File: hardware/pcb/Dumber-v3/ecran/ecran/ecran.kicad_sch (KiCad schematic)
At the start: 14 parts, among them J1 TE 1-84981-0

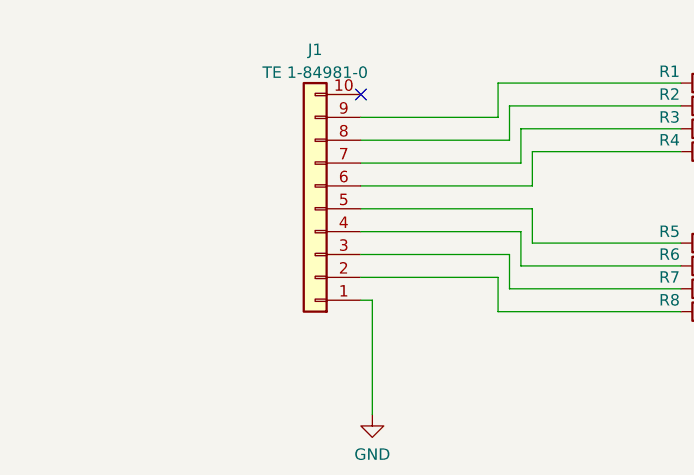
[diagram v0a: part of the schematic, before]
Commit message: asservissement moteur de base OK
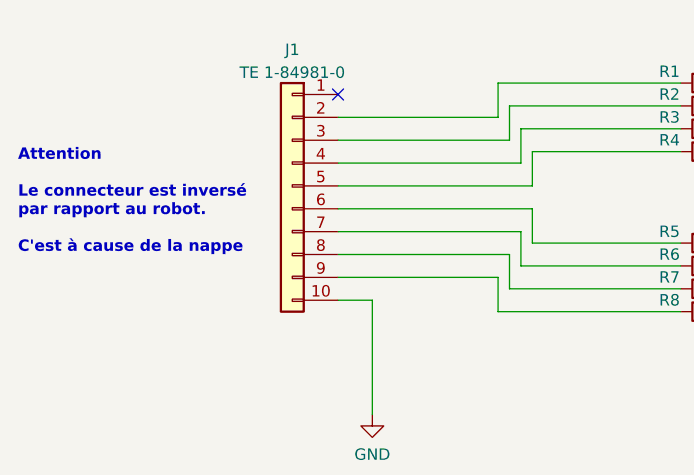
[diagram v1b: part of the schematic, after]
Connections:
- net GND: now also J1.10 (Pin_10); no longer J1.1 (Pin_1)
- net at R8.1: now also J1.9 (Pin_9); no longer J1.2 (Pin_2)
- net at R1.1: now also J1.2 (Pin_2); no longer J1.9 (Pin_9)
- net at R2.1: now also J1.3 (Pin_3); no longer J1.8 (Pin_8)
- net at R6.1: now also J1.7 (Pin_7); no longer J1.4 (Pin_4)
- net at R4.1: now also J1.5 (Pin_5); no longer J1.6 (Pin_6)
- net at R7.1: now also J1.8 (Pin_8); no longer J1.3 (Pin_3)
- net at R5.1: now also J1.6 (Pin_6); no longer J1.5 (Pin_5)
- net at R3.1: now also J1.4 (Pin_4); no longer J1.7 (Pin_7)
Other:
- note added: "Attention Le connecteur est inversé par rapport au robot. C'est à cause de la nappe"
- moved on the sheet: J1
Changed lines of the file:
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@@
     (company "INSA - GEI")
   )
+  (no_connect (at 58.42 63.5))
   (no_connect (at 175.26 86.36))
-  (no_connect (at 60.96 63.5))
   (wire (pts (xy 148.59 83.82) (xy 119.38 83.82))
     (stroke (width 0) (type default) (color 0 0 0 0))
@@
     (stroke (width 0) (type default) (color 0 0 0 0))
   )
+  (wire (pts (xy 58.42 81.28) (xy 77.47 81.28))
+    (stroke (width 0) (type default) (color 0 0 0 0))
+  )
   (wire (pts (xy 62.23 86.36) (xy 62.23 99.06))
     (stroke (width 0) (type default) (color 0 0 0 0))
   )
-  (wire (pts (xy 60.96 76.2) (xy 80.01 76.2))
-    (stroke (width 0) (type default) (color 0 0 0 0))
-  )
-  (wire (pts (xy 60.96 71.12) (xy 78.74 71.12))
-    (stroke (width 0) (type default) (color 0 0 0 0))
-  )
   (wire (pts (xy 104.14 82.55) (xy 110.49 82.55))
     (stroke (width 0) (type default) (color 0 0 0 0))
   )
-  (wire (pts (xy 60.96 66.04) (xy 76.2 66.04))
-    (stroke (width 0) (type default) (color 0 0 0 0))
-  )
   (wire (pts (xy 78.74 67.31) (xy 96.52 67.31))
     (stroke (width 0) (type default) (color 0 0 0 0))
@@
     (stroke (width 0) (type default) (color 0 0 0 0))
   )
-  (wire (pts (xy 60.96 68.58) (xy 77.47 68.58))
-    (stroke (width 0) (type default) (color 0 0 0 0))
-  )
   (wire (pts (xy 148.59 66.04) (xy 175.26 66.04))
     (stroke (width 0) (type default) (color 0 0 0 0))
@@
     (stroke (width 0) (type default) (color 0 0 0 0))
   )
-  (wire (pts (xy 60.96 81.28) (xy 77.47 81.28))
-    (stroke (width 0) (type default) (color 0 0 0 0))
-  )
   (wire (pts (xy 76.2 87.63) (xy 96.52 87.63))
     (stroke (width 0) (type default) (color 0 0 0 0))
   )
-  (wire (pts (xy 60.96 73.66) (xy 80.01 73.66))
-    (stroke (width 0) (type default) (color 0 0 0 0))
-  )
   (wire (pts (xy 153.67 76.2) (xy 175.26 76.2))
     (stroke (width 0) (type default) (color 0 0 0 0))
@@
     (stroke (width 0) (type default) (color 0 0 0 0))
   )
+  (wire (pts (xy 58.42 66.04) (xy 76.2 66.04))
+    (stroke (width 0) (type default) (color 0 0 0 0))
+  )
+  (wire (pts (xy 58.42 71.12) (xy 78.74 71.12))
+    (stroke (width 0) (type default) (color 0 0 0 0))
+  )
+  (wire (pts (xy 58.42 76.2) (xy 80.01 76.2))
+    (stroke (width 0) (type default) (color 0 0 0 0))
+  )
   (wire (pts (xy 149.86 81.28) (xy 114.3 81.28))
     (stroke (width 0) (type default) (color 0 0 0 0))
@@
     (stroke (width 0) (type default) (color 0 0 0 0))
   )
-  (wire (pts (xy 60.96 78.74) (xy 78.74 78.74))
-    (stroke (width 0) (type default) (color 0 0 0 0))
-  )
   (wire (pts (xy 151.13 71.12) (xy 175.26 71.12))
     (stroke (width 0) (type default) (color 0 0 0 0))
@@
     (stroke (width 0) (type default) (color 0 0 0 0))
   )
+  (wire (pts (xy 58.42 78.74) (xy 78.74 78.74))
+    (stroke (width 0) (type default) (color 0 0 0 0))
+  )
   (wire (pts (xy 119.38 83.82) (xy 119.38 87.63))
     (stroke (width 0) (type default) (color 0 0 0 0))
@@
     (stroke (width 0) (type default) (color 0 0 0 0))
   )
+  (wire (pts (xy 58.42 73.66) (xy 80.01 73.66))
+    (stroke (width 0) (type default) (color 0 0 0 0))
+  )
   (wire (pts (xy 104.14 62.23) (xy 140.97 62.23))
     (stroke (width 0) (type default) (color 0 0 0 0))
@@
     (stroke (width 0) (type default) (color 0 0 0 0))
   )
-  (wire (pts (xy 60.96 83.82) (xy 76.2 83.82))
-    (stroke (width 0) (type default) (color 0 0 0 0))
-  )
   (wire (pts (xy 149.86 68.58) (xy 175.26 68.58))
     (stroke (width 0) (type default) (color 0 0 0 0))
@@
     (stroke (width 0) (type default) (color 0 0 0 0))
   )
+  (wire (pts (xy 58.42 83.82) (xy 76.2 83.82))
+    (stroke (width 0) (type default) (color 0 0 0 0))
+  )
   (wire (pts (xy 104.14 64.77) (xy 142.24 64.77))
     (stroke (width 0) (type default) (color 0 0 0 0))
@@
     (stroke (width 0) (type default) (color 0 0 0 0))
   )
-  (wire (pts (xy 60.96 86.36) (xy 62.23 86.36))
-    (stroke (width 0) (type default) (color 0 0 0 0))
-  )
   (wire (pts (xy 152.4 76.2) (xy 152.4 73.66))
     (stroke (width 0) (type default) (color 0 0 0 0))
@@
     (stroke (width 0) (type default) (color 0 0 0 0))
   )
+  (wire (pts (xy 58.42 68.58) (xy 77.47 68.58))
+    (stroke (width 0) (type default) (color 0 0 0 0))
+  )
+  (wire (pts (xy 58.42 86.36) (xy 62.23 86.36))
+    (stroke (width 0) (type default) (color 0 0 0 0))
+  )
   (wire (pts (xy 151.13 78.74) (xy 110.49 78.74))
     (stroke (width 0) (type default) (color 0 0 0 0))
@@
   (wire (pts (xy 104.14 69.85) (xy 146.05 69.85))
     (stroke (width 0) (type default) (color 0 0 0 0))
+  )
+  (text "Attention\n\nLe connecteur est inversé \npar rapport au robot.\n\nC'est à cause de la nappe"
+    (at 22.86 81.28 0)
+    (effects (font (size 1.27 1.27) (thickness 0.254) bold) (justify left bottom))
   )
   (symbol (lib_id "power:GND") (at 62.23 99.06 0) (unit 1)
@@
     (pin "1")
   )
-  (symbol (lib_id "Connector_Generic:Conn_01x10") (at 55.88 76.2 180) (unit 1)
-    (in_bom yes) (on_board yes) (fields_autoplaced)
-    (property "Reference" "J1" (id 0) (at 55.88 58.5302 0))
-    (property "Value" "TE 1-84981-0" (id 1) (at 55.88 61.0671 0))
-    (property "Footprint" "INSA:TE 1-84981-0" (id 2) (at 55.88 76.2 0)
-      (effects (font (size 1.27 1.27)) hide)
-    )
-    (property "Datasheet" "~" (id 3) (at 55.88 76.2 0)
-      (effects (font (size 1.27 1.27)) hide)
-    )
+  (symbol (lib_id "Connector_Generic:Conn_01x10") (at 53.34 73.66 0) (mirror y) (unit 1)
+    (in_bom yes) (on_board yes) (fields_autoplaced)
+    (property "Reference" "J1" (id 0) (at 53.34 58.5302 0))
+    (property "Value" "TE 1-84981-0" (id 1) (at 53.34 61.0671 0))
+    (property "Footprint" "INSA:TE 1-84981-0" (id 2) (at 53.34 73.66 0)
+      (effects (font (size 1.27 1.27)) hide)
+    )
+    (property "Datasheet" "~" (id 3) (at 53.34 73.66 0)
+      (effects (font (size 1.27 1.27)) hide)
+    )
